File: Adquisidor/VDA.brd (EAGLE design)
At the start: 100 x 90 mm, 109 parts, among them J1 USB-2.0, J3 FTSH-107-01-L-DV-K-A, SW1 DSHP03TSGER, U1 SN74LVC1G175, U2 CP2102N-28, U3 STM32F373CBT6, U4 LP5907MFX-3.3/NOPB, U5 ISO7721DR, U6 LP5907MFX-3.3/NOPB, U7 TL072, U8 LM13700, U9 REF3433IDBVR

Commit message: layout avanzado
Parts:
- removed C32: 470n, Property-standar:C_0603
- removed C39: 4u7, Property-standar:C_0603
- removed C40: 100n, Property-standar:C_0603
- removed C41: 10u, Property-standar:C_0603
- removed U9: REF3433IDBVR, Power-Supply:SOT23-6
- added C42: 1u, Property-standar:C_0603
- added C43: 100n, Property-standar:C_0603
- added D1, D13, D14, D15, D16, D17, D6, D7, D8, D9: 1N4148, Property-standar:SOD123W
- added J2: CONVERT-2X6-2.54MM-FEMALE, property-connectors:CONN-VERT-2.54MM-2X6-FEMALE
- added J4: CONVERT-1X4-2.54MM-MALE_HOLES, property-connectors:1X04
- added J5: F0504-H-05-10G-R, property-connectors:F0504-H-05-10G-R
- added Q1, Q2: BC856, Property-standar:SOT-23
- added R30: 33k, Property-standar:R_0603
- added R31: 3k9, Property-standar:R_0603
- added R32: 100, Property-standar:R_0603
- added R33: 500, Property-standar:RTRIM64W
- added R34: 1k, Property-standar:R_0603
- added R35, R37: TBD, Property-standar:R_0603
- added SJ3: (no value), jumper:SJ
- added TP10, TP5, TP6, TP7, TP8, TP9: TPTP16R, property-pads:TP16R
- C29, C30: value 47n -> 100n
- C31: value 3.3u -> 47n
- R10: value 2k -> 150
- R11: value 2k -> 100
- R12: value 30k -> 100k
- R13: value 10k -> TBD
- R14: value 30k -> DNP
- R29: value (none) -> 10k
- R3: value 10M -> TBD; device Property-standar:R_0603 -> Property-standar:RTRIM64W
- R7: value 10M -> TBD
- R9: value 2k -> 33k
- SJ1: device jumper:SJ_2 -> property-pads:SJ_2S
- SJ2: device jumper:SJ -> property-pads:SJ_2S
- moved R27 161.0 mm to (78.1, 59.1), turned to 180 degrees
- moved SJ1 160.7 mm to (73.7, 62.9), turned to 270 degrees
- moved R13 137.0 mm to (19.7, 45.7), turned to 90 degrees
- moved C36 134.9 mm to (41.9, 42.5), turned to 90 degrees
- moved C35 133.2 mm to (43.8, 33.0), turned to 180 degrees
- moved R12 131.0 mm to (21.0, 40.6)
- moved U8 130.4 mm to (40.0, 37.5), turned to 90 degrees
- moved D10 130.3 mm to (78.1, 74.3), turned to 270 degrees
- moved D12 129.6 mm to (83.2, 74.3), turned to 270 degrees
- moved R5 123.7 mm to (78.1, 71.8), turned to 90 degrees
- moved R36 121.1 mm to (83.2, 71.8), turned to 90 degrees
- moved C31 118.6 mm to (21.0, 42.5)
- moved R11 118.2 mm to (45.7, 27.3), turned to 90 degrees
- moved R14 116.5 mm to (26.7, 29.8), turned to 270 degrees
- moved R10 107.6 mm to (31.8, 25.4), turned to 90 degrees
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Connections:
- net ON_MODE renamed SW_1
- net RS_MODE renamed SW_2
- net SP_MODE renamed SW_3
- removed net DAC_OUT: R14.1
- removed net GND1: C30.P$2, R7.1, R9.2, U7.1
- removed net LED_ACQ: D12.K
- removed net LED_PWR: D10.K
- removed net MANUAL_GAIN: R29.P$3
- removed net PV: U3.28
- removed net SP1: U3.19
- new net ACQ_LED: J5.P$4, R36.1, U3.42
- new net DAC1_CH1: R9.2, TP7.TP, U3.13
- new net DAC1_CH2: J2.9, U3.14
- new net DAC2_CH1: J2.5, U3.15
- new net I_ABC: Q1.3, U8.1
- new net N$20: R33.2, R33.3, U8.4
- new net N$21: Q2.3, U8.2
- new net N$22: R32.1, R33.1
- new net N$23: J5.P$2, SJ1.COM
- new net N$24: D6.A, Q2.1, R10.2
- new net N$27: R35.2, R37.1, U7.9
- new net OUT_CHARGE_AMP: C30.P$2, R30.1, R6.1, TP8.TP, U7.1
- new net OUT_OTA: C31.P$2, R12.1, U7.13, U8.5
- new net POWER_LED: J5.P$5, U3.43
- new net SDADC1_CH4: J2.3, U3.20
- new net SDADC1_CH5: D16.A, D17.C, R37.2, TP6.TP, U3.19, U7.8
- new net SDADC1_CH6: R29.P$2, TP10.TP, U3.18
- new net SDADC1_CH7: TP9.TP, U3.22
- new net SDADC1_CH8: J2.4, U3.21
- new net SDADC3_CH7: J2.7, U3.27
- new net SDADC3_CH8: J2.8, U3.26
- new net VREF_SDADC: C42.P$1, C43.P$1, SJ3.2, U3.25
- net +3V3: now also J4.4, SJ1.NO; no longer R36.1, R5.1
- net +3V3A: now also D16.C, R13.2, R14.2, R29.P$3, SJ3.1; no longer R29.P$1, SJ2.1, U3.25
- net +5V: now also D1.C, D13.C, D9.C, J2.1, J2.11, R34.2, R5.1, SJ1.NC; no longer C41.P$1, U9.3, U9.4
- net -5V: now also D7.A, D8.A, J2.12, J2.2, U8.15; no longer R13.2
- net BOOT0: now also J5.P$3, R22.1, U1.4
- net GND: now also C42.P$2, C43.P$2, D10.K, D12.K, D17.A, J2.10, J2.6, J4.2, J5.P$1, J5.P$7, J5.P$8, R10.1, R11.2, R29.P$1, R31.2, R7.1, SJ2.NO, U$6.1, U7.5; no longer C31.P$2, C39.P$2, C40.P$2, C41.P$2, R12.2, R29.P$2, SJ1.3, U9.1, U9.2
- net JCLK: now also J4.3
- net JTMS: now also J4.1
- net N$10: now also Q1.1, U7.7; no longer C32.P$1, R10.1, U7.14
- net N$11: now also Q2.2, R34.1; no longer C32.P$2, R11.1, U7.13
- net N$12: now also D1.A, D6.C; no longer R13.1, U8.8
- net N$13: now also R13.1, R3.1; no longer R14.2, U8.1
- net N$16: now also D13.A, D14.C, D15.A, D8.C
- net N$17: now also D14.A, D15.C, D7.C, D9.A, SJ2.NC; no longer SJ1.1
- net N$18: now also R3.2, U7.10; no longer R22.1, U1.4
- net N$19: now also R30.2, R31.1, U8.3; no longer C39.P$1, C40.P$1, SJ2.2, U9.5, U9.6
- net N$2: now also C31.P$1, R12.2, R35.1, TP5.TP, U7.14; no longer C29.P$1, R23.1, R3.2, U7.3
- net N$3: now also C29.P$1, R23.1, U7.3; no longer R3.1
- net N$5: now also R3.3; no longer R6.1
- net N$6: now also SJ2.COM; no longer SJ1.2, U$6.1
- net N$7: now also Q1.2, R14.1, U7.6; no longer C31.P$1, R10.2, R11.2
- net N$9: now also R11.1, R32.2; no longer R12.1, U8.5, U8.7
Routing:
- net +5V: track 27.1 -> 340.2 mm, vias 0 -> 8
- net -5V: track 29.4 -> 231.2 mm, vias 0 -> 5
- net DAC1_CH1: track 0.00 -> 87.6 mm, vias 0 -> 4
- net SDADC1_CH5: track 0.00 -> 83.8 mm, vias 0 -> 2
- net SDADC3_CH8: track 0.00 -> 50.7 mm, vias 0 -> 2
- net GND: track 26.3 -> 75.6 mm, vias 19 -> 47
- net SDADC3_CH7: track 0.00 -> 48.0 mm, vias 0 -> 2
- net SDADC1_CH8: track 0.00 -> 46.4 mm, vias 0 -> 2
- net SDADC1_CH4: track 0.00 -> 43.2 mm, vias 0 -> 2
- net USART_RX: track 41.7 -> 82.7 mm
- net DAC2_CH1: track 0.00 -> 37.8 mm, vias 0 -> 2
- net SDADC1_CH6: track 0.00 -> 36.0 mm, vias 0 -> 2
- net N$16: track 0.00 -> 33.2 mm, vias 0 -> 2
- net USART_TX: track 50.8 -> 83.9 mm
- net BOOT0: track 0.00 -> 32.2 mm
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- added copper zone on layer 1, net GND-1
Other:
- board text added: "+3V3"
- board text added: "ACQ"
- board text added: "Diseñado por Leandro Zabala"
- board text added: "GND"
- board text added: "PROG"
- board text added: "PWR"
- board text added: "SWCLK"
- board text added: "SWDIO"

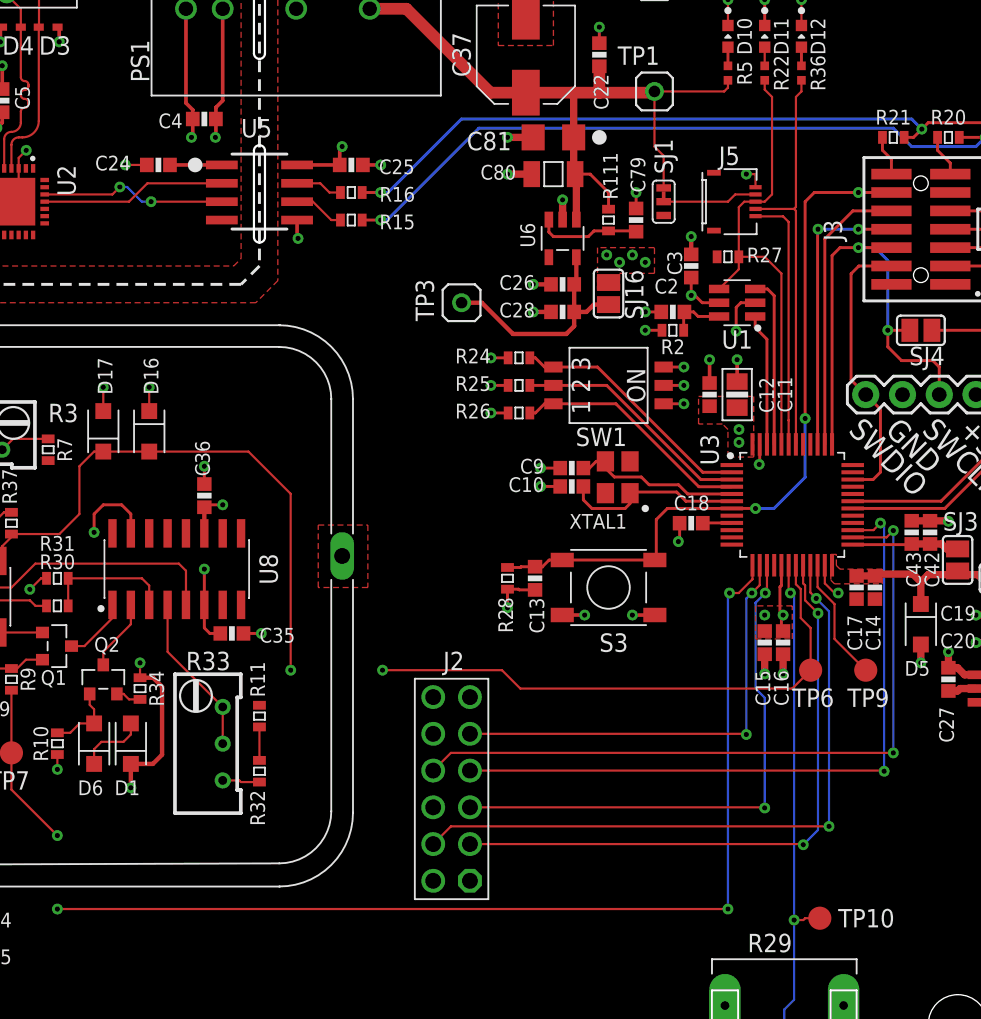
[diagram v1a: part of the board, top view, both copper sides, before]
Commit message: cambio de conector para expansion
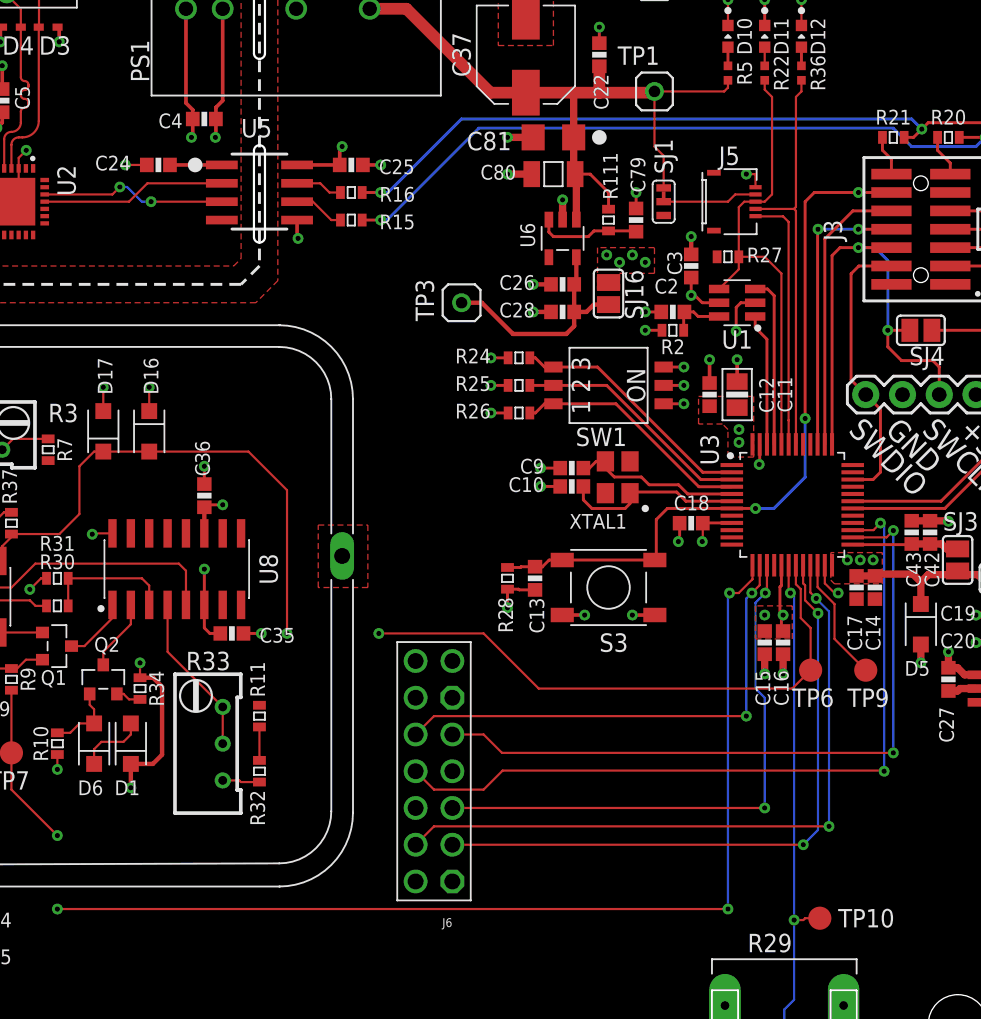
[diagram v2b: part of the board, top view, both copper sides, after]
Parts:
- removed J2: CONVERT-2X6-2.54MM-FEMALE, property-connectors:CONN-VERT-2.54MM-2X6-FEMALE
- added J6: CONVERT-2X7-2.54MM-FEMALE, property-connectors:CONN-VERT-2.54MM-2X7-FEMALE
- R35: value TBD -> 1k
- R37: value TBD -> 2k2
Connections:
- net +3V3A: now also J6.12, J6.7
- net +5V: now also J6.1, J6.14; no longer J2.1, J2.11
- net -5V: now also J6.13, J6.2, U8.16; no longer J2.12, J2.2, U8.15
- net DAC1_CH2: now also J6.10; no longer J2.9
- net DAC2_CH1: now also J6.5; no longer J2.5
- net GND: now also J6.11, J6.6; no longer J2.10, J2.6
- net SDADC1_CH4: now also J6.3; no longer J2.3
- net SDADC1_CH8: now also J6.4; no longer J2.4
- net SDADC3_CH7: now also J6.8; no longer J2.7
- net SDADC3_CH8: now also J6.9; no longer J2.8
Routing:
- net SDADC3_CH7: track 48.0 -> 52.9 mm
- net -5V: track 231.2 -> 226.8 mm
- net DAC1_CH2: track 31.2 -> 34.2 mm
- net SDADC1_CH5: track 83.8 -> 82.4 mm
- net SDADC3_CH8: track 50.7 -> 49.4 mm
- net +3V3A: track 17.6 -> 18.9 mm, vias 3 -> 7
- net SDADC1_CH8: track 46.4 -> 47.7 mm
- net DAC2_CH1: track 37.8 -> 39.0 mm
- net SDADC1_CH4: track 43.2 -> 44.4 mm
- added copper zone on layer 15, net +3V3A

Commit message: layout terminado
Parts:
- R3, R33: device Property-standar:RTRIM64W -> Property-standar:RV3.2X4
- moved R7 12.1 mm to (19.1, 47.0)
- moved R13 6.63 mm to (26.0, 47.6), turned to 0 degrees
- moved R3 4.62 mm to (21.0, 45.7), turned to 90 degrees
- moved R33 2.01 mm to (41.3, 23.5), turned to 90 degrees
- moved R11 0.63 mm to (46.4, 27.3)
- moved R32 0.63 mm to (46.4, 23.5)
- turned J6 to 270 degrees
- renumbered U$6 to J2
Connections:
- net +3V3A: now also J6.14; no longer J6.12
- net +5V: now also J6.9; no longer J6.14
- net -5V: now also J6.8; no longer J6.13
- net DAC1_CH2: now also J6.12; no longer J6.10
- net GND: now also J6.13; no longer J6.11
- net SDADC3_CH7: now also J6.10; no longer J6.8
- net SDADC3_CH8: now also J6.11; no longer J6.9
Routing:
- net +5V: track 340.2 -> 388.5 mm, vias 8 -> 9
- net -5V: track 226.8 -> 269.8 mm, vias 5 -> 6
- net SDADC1_CH8: track 47.7 -> 36.6 mm
- net N$2: track 30.6 -> 21.6 mm
- net SDADC3_CH8: track 49.4 -> 57.0 mm
- net DAC1_CH2: track 34.2 -> 39.6 mm
- net GND: track 75.6 -> 81.0 mm, vias 47 -> 50
- net SDADC1_CH4: track 44.4 -> 39.4 mm
- net N$20: track 11.2 -> 13.5 mm
- net N$50: track 4.46 -> 6.74 mm
- net N$22: track 2.59 -> 4.56 mm
- net N$18: track 7.69 -> 9.60 mm
- net N$5: track 3.49 -> 1.68 mm
- net N$13: track 3.49 -> 1.98 mm
- net VUSB: track 30.0 -> 31.4 mm, vias 5 -> 6
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- added copper zone on layer 15, net +3V3
- added copper zone on layer 16, net GND
- added copper zone on layer 16, net GND-1
